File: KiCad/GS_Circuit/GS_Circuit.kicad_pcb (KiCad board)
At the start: 2 copper layers, 80 x 80 mm, 11 parts, among them J1 AVR-ISP-6, U2 ATtiny85V-10P

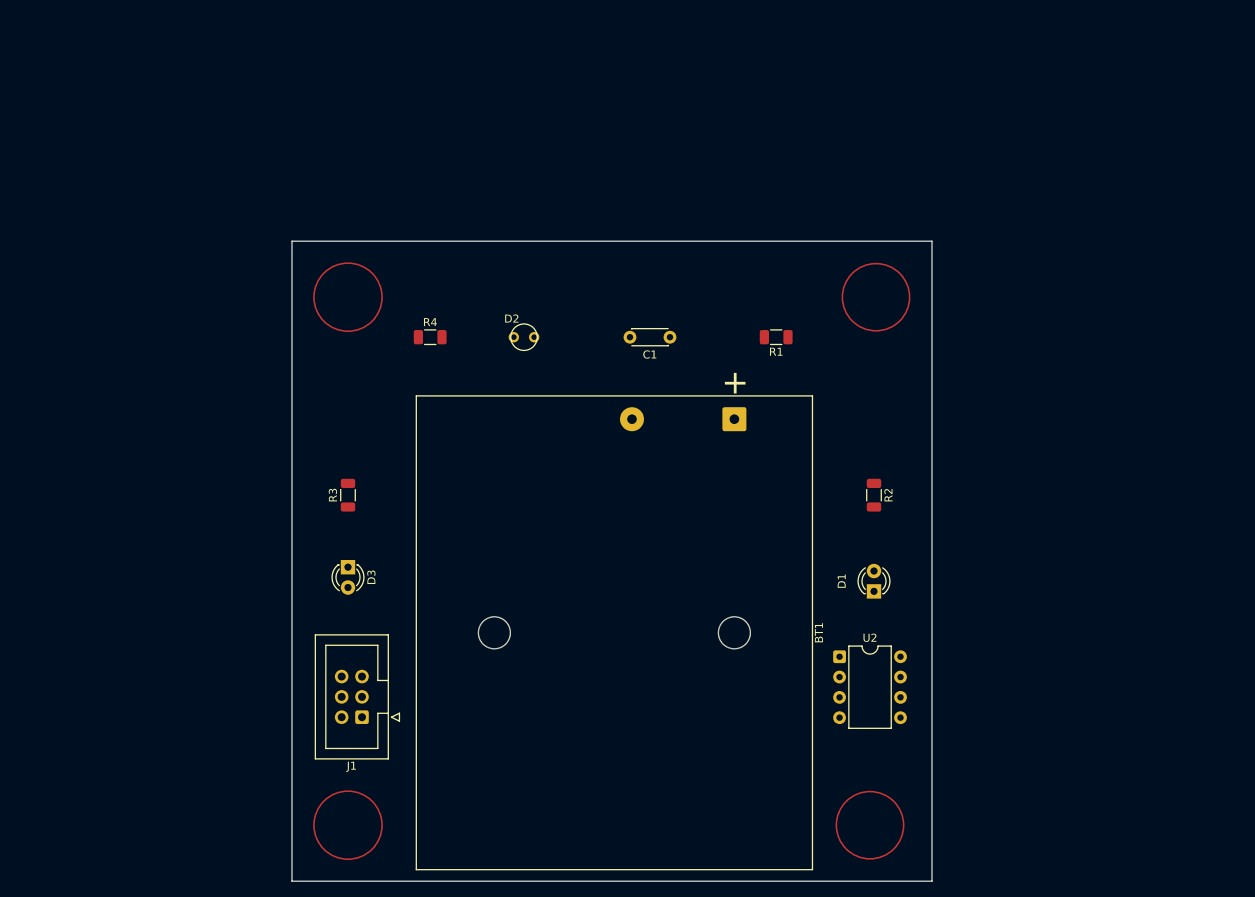
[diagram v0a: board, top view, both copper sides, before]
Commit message: First try foot print
Added library components with foot prints.  (photo sensor and switches).

First draft at PCB layout.
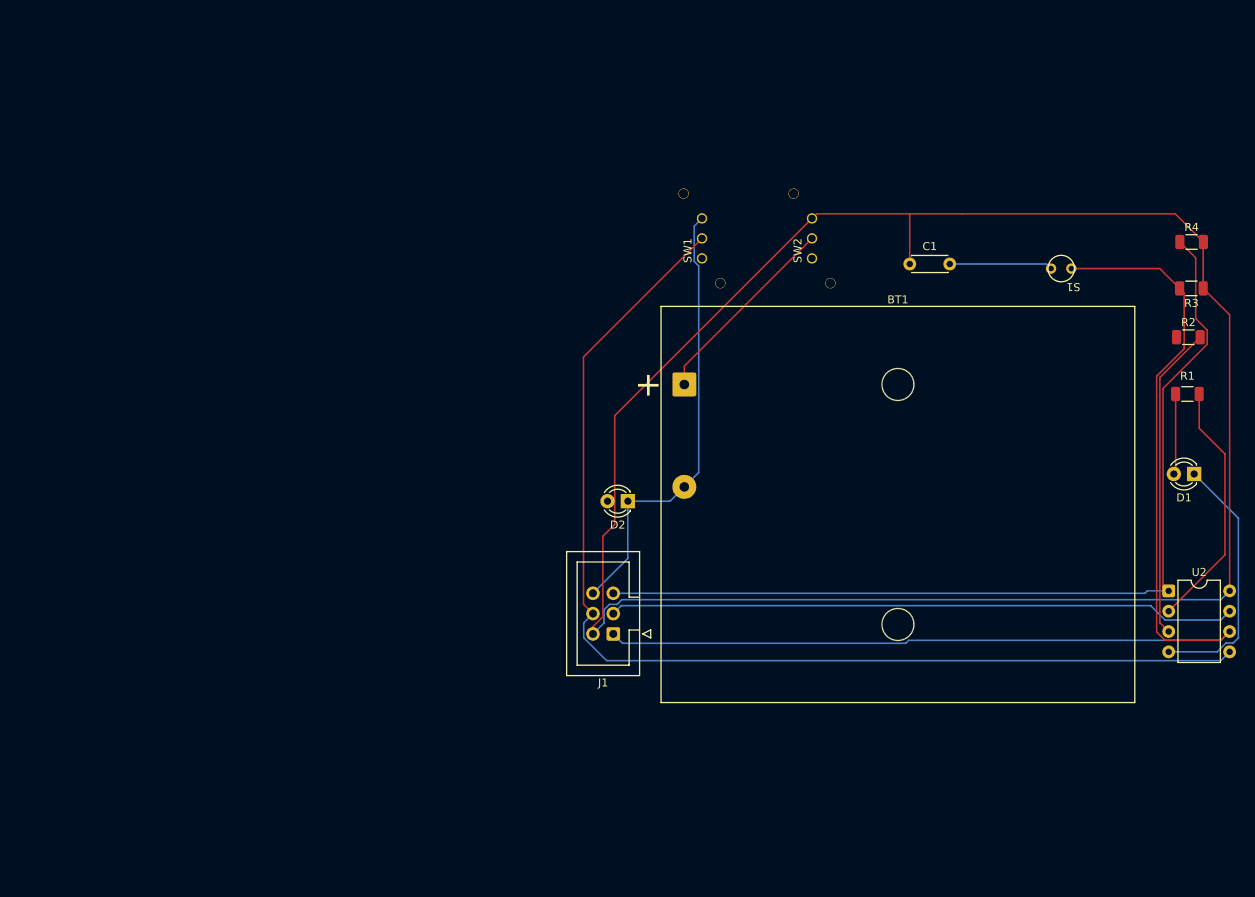
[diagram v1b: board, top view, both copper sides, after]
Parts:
- removed D3: LED, TLHG4600, TLHY4600, TLHY4600, TLHF4601, LED_THT:LED_D3.0mm
- added S1: TEPT 4400, Library:TEPT4400, F.Cu at (147.4, 53.4)
- added SW1: SW_Push, Library:LC 1258, F.Cu at (101.2, 49.6)
- added SW2: SW_SPST, Library:LC 1258, F.Cu at (115.0, 49.6)
- D2: value TEPT 4400 -> LED, TLHG4600, TLHY4600, TLHY4600, TLHF4601; footprint Library:TEPT4400 -> LED_THT:LED_D3.0mm
- R3: value R_US -> 10K
- R4: value 10K -> R_US
- moved R3 108.5 mm to (162.4, 55.9), turned to 180 degrees
- moved R4 95.9 mm to (162.4, 50.1)
- moved R1 51.9 mm to (161.9, 69.1), turned to 0 degrees
- moved R2 44.0 mm to (162.1, 62.0), turned to 0 degrees
- moved D1 42.6 mm to (162.8, 79.1), turned to 180 degrees
- moved U2 42.0 mm to (159.6, 93.7)
- moved J1 33.1 mm to (90.2, 99.1)
- moved C1 31.3 mm to (127.2, 52.9), turned to 0 degrees
- moved D2 25.0 mm to (92.0, 82.5), turned to 180 degrees
- moved BT1 7.62 mm to (99.0, 67.9), turned to 0 degrees
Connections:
- D2 pad 1: /MISO -> GND
- D2 pad 2: GND -> Net-(D2-A)
- R1 pad 1: /~{RST} -> Net-(D1-A)
- R1 pad 2: VCC -> Net-(U2-XTAL1/PB3)
- R2 pad 1: Net-(D1-A) -> Net-(D2-A)
- R2 pad 2: Net-(U2-XTAL1/PB3) -> Net-(U2-XTAL2/PB4)
- R3 pad 1: Net-(D3-A) -> VCC
- R3 pad 2: Net-(U2-XTAL2/PB4) -> /MISO
- R4 pad 1: VCC -> /~{RST}
- R4 pad 2: /MISO -> VCC
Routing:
- net VCC: track 0.00 -> 247.9 mm
- net /MISO: track 0.00 -> 147.3 mm
- net /MOSI: track 0.00 -> 139.4 mm
- net /~{RST}: track 0.00 -> 117.2 mm
- net GND: track 0.00 -> 101.2 mm
- net /SCK: track 0.00 -> 78.7 mm
- net Net-(U2-XTAL2/PB4): track 0.00 -> 39.3 mm
- net Net-(U2-XTAL1/PB3): track 0.00 -> 31.4 mm
- net Net-(BT1-+): track 0.00 -> 24.9 mm
- net Net-(D1-A): track 0.00 -> 10.1 mm
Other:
- board outline removed

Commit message: MD Electron Feedback 1
-Changed Library Structure
-Fixed switch footprint issue
-Added PCB over all footprint and layout
-Moved silkscreen labels
-
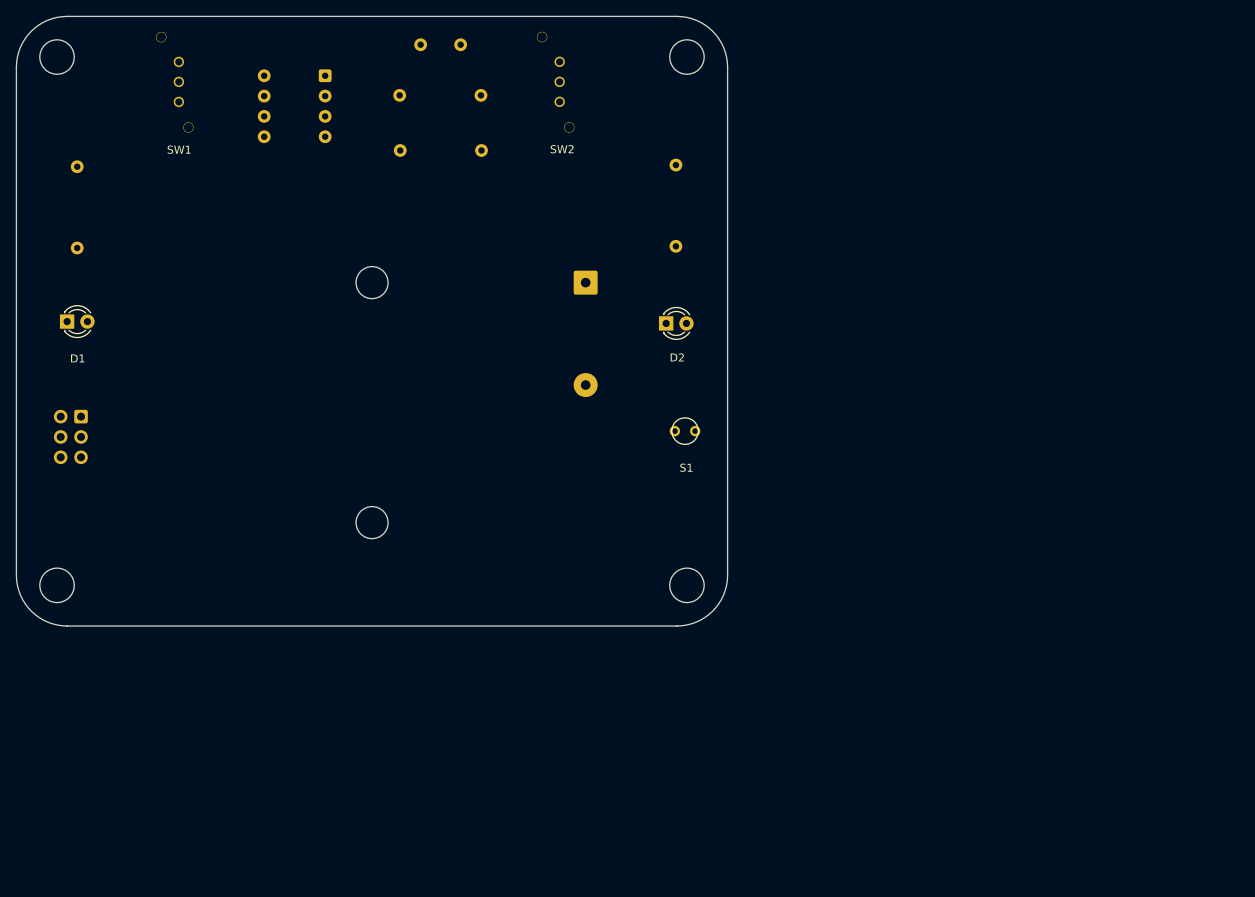
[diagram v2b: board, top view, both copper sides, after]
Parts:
- added H1: MountingHole, MountingHole:MountingHole_4.3mm_M4, F.Cu at (20.6, 93.0)
- added H2: MountingHole, MountingHole:MountingHole_4.3mm_M4, F.Cu at (20.6, 27.0)
- added H3: MountingHole, MountingHole:MountingHole_4.3mm_M4, F.Cu at (99.4, 27.0)
- added H4: MountingHole, MountingHole:MountingHole_4.3mm_M4, F.Cu at (99.4, 93.0)
- BT1, C1, J1, U2: moved to B.Cu
- R1, R2, R3, R4: footprint Capacitor_SMD:C_1206_3216Metric -> Resistor_THT:R_Axial_DIN0207_L6.3mm_D2.5mm_P10.16mm_Horizontal; moved to B.Cu
- S1: footprint Library:TEPT4400 -> GS_Parts:TEPT4400
- SW1, SW2: footprint Library:LC 1258 -> GS_Parts:LC 1258
- moved D1 142.2 mm to (21.9, 60.0), turned to 0 degrees
- moved R1 140.0 mm to (23.1, 50.9), turned to 90 degrees
- moved U2 123.5 mm to (54.1, 29.3), turned to 180 degrees
- moved R4 100.7 mm to (63.5, 31.8)
- moved R3 90.4 mm to (73.7, 38.7)
- moved J1 71.9 mm to (23.6, 71.9)
- moved SW1 68.3 mm to (35.9, 30.1)
- moved R2 65.1 mm to (98.0, 50.6), turned to 90 degrees
- moved C1 62.5 mm to (71.1, 25.4), turned to 180 degrees
- moved S1 53.6 mm to (97.9, 73.7), turned to 0 degrees
- moved SW2 37.1 mm to (83.5, 30.1)
- moved D2 22.7 mm to (96.8, 60.3), turned to 0 degrees
- moved BT1 17.7 mm to (86.7, 55.2), turned to 180 degrees
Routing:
- net VCC: track 247.9 -> 0.00 mm
- net /MISO: track 147.3 -> 0.00 mm
- net /MOSI: track 139.4 -> 0.00 mm
- net /~{RST}: track 117.2 -> 0.00 mm
- net GND: track 101.2 -> 0.00 mm
- net /SCK: track 78.7 -> 0.00 mm
- net Net-(U2-XTAL2/PB4): track 39.3 -> 0.00 mm
- net Net-(U2-XTAL1/PB3): track 31.4 -> 0.00 mm
- net Net-(BT1-+): track 24.9 -> 0.00 mm
- net Net-(D1-A): track 10.1 -> 0.00 mm
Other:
- board outline added: 88.9 x 76.2 mm
